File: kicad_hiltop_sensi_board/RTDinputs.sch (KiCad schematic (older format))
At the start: 0 parts

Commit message: updated sensi board for LBBC 04/09/19
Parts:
- added C1, C2, C3, C30, C31, C32, C33, C4, C5, C6, C7, C8: 100n, symbol device:C
- added J10, J11, J12, J4, J5, J7, J8, J9: Screw_Terminal_01x02, symbol Connector:Screw_Terminal_01x02
- added JP10, JP2, JP4, JP8: Jumper_NC_Dual, symbol device:Jumper_NC_Dual
- added JP11, JP12, JP13, JP3, JP5, JP6, JP7, JP9: Jumper_NC_Small, symbol device:Jumper_NC_Small
- added R1, R2, R5, R6: 470, symbol device:R
- added R12, R3, R4, R7: 10k, symbol device:R
- added U10, U11, U12, U9: MAX31865, symbol Devtank:MAX31865
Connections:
- new net: R2.1, U10.1 (BIAS), U10.2 (REFIN+)
- new net: R2.2, U10.3 (REFIN-), U10.4 (ISENSOR)
- new net: C3.1, J8.2 (Pin_2), JP7.1, U10.8 (RTDIN-)
- new net: C3.2, J5.1 (Pin_1), JP5.2, U10.7 (RTDIN+)
- new net: J5.2 (Pin_2), JP4.1, JP5.1, U10.5 (FORCE+)
- new net: JP4.2, U10.6 (FORCE2)
- new net: J8.1 (Pin_1), JP7.2, U10.9 (FORCE-)
- new net: R6.1, U12.1 (BIAS), U12.2 (REFIN+)
- new net: R6.2, U12.3 (REFIN-), U12.4 (ISENSOR)
- new net: J10.2 (Pin_2), JP10.1, JP11.1, U12.5 (FORCE+)
- new net: JP10.2, U12.6 (FORCE2)
- new net: C30.2, J10.1 (Pin_1), JP11.2, U12.7 (RTDIN+)
- new net: C30.1, J12.2 (Pin_2), JP13.1, U12.8 (RTDIN-)
- new net: J12.1 (Pin_1), JP13.2, U12.9 (FORCE-)
- new net: R1.1, U9.1 (BIAS), U9.2 (REFIN+)
- new net: R1.2, U9.3 (REFIN-), U9.4 (ISENSOR)
- new net: J4.2 (Pin_2), JP2.1, JP3.1, U9.5 (FORCE+)
- new net: JP2.2, U9.6 (FORCE2)
- new net: C1.2, J4.1 (Pin_1), JP3.2, U9.7 (RTDIN+)
- new net: C1.1, J7.2 (Pin_2), JP6.1, U9.8 (RTDIN-)
- new net: J7.1 (Pin_1), JP6.2, U9.9 (FORCE-)
- new net: R5.1, U11.1 (BIAS), U11.2 (REFIN+)
- new net: R5.2, U11.3 (REFIN-), U11.4 (ISENSOR)
- new net: J9.2 (Pin_2), JP8.1, JP9.1, U11.5 (FORCE+)
- new net: JP8.2, U11.6 (FORCE2)
- new net: C7.2, J9.1 (Pin_1), JP9.2, U11.7 (RTDIN+)
- new net: C7.1, J11.2 (Pin_2), JP12.1, U11.8 (RTDIN-)
- new net: J11.1 (Pin_1), JP12.2, U11.9 (FORCE-)
- new net +3V3: C2.1, C31.1, C32.1, C33.1, C4.1, C5.1, C6.1, C8.1, R12.1, R3.1, R4.1, R7.1, U10.19 (DVDD), U10.20 (VDD), U11.19 (DVDD), U11.20 (VDD), U12.19 (DVDD), U12.20 (VDD), U9.19 (DVDD), U9.20 (VDD)
- new net CS1: R4.2, U10.13 (~CS)
- new net CS2: R12.2, U12.13 (~CS)
- new net CS3: R3.2, U9.13 (~CS)
- new net CS4: R7.2, U11.13 (~CS)
- new net GND: C2.2, C31.2, C32.2, C33.2, C4.2, C5.2, C6.2, C8.2, JP10.3, JP2.3, JP4.3, JP8.3, U10.10 (GND2), U10.15 (DGND), U10.16 (GND1), U10.21 (EP), U11.10 (GND2), U11.15 (DGND), U11.16 (GND1), U11.21 (EP), U12.10 (GND2), U12.15 (DGND), U12.16 (GND1), U12.21 (EP), U9.10 (GND2), U9.15 (DGND), U9.16 (GND1), U9.21 (EP)
- new net INT1: U10.18 (~DRDY)
- new net INT2: U12.18 (~DRDY)
- new net INT3: U9.18 (~DRDY)
- new net INT4: U11.18 (~DRDY)
- new net MISO: U10.14 (SDO), U11.14 (SDO), U12.14 (SDO), U9.14 (SDO)
- new net MOSI: U10.11 (SDI), U11.11 (SDI), U12.11 (SDI), U9.11 (SDI)
- new net SCK: U10.12 (SCLK), U11.12 (SCLK), U12.12 (SCLK), U9.12 (SCLK)
- no-connect marks 0 -> 4

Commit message: LBBC sensi board upto date schematic and footprints
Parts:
- C1, C2, C3, C30, C31, C32, C33, C4, C5, C6, C7, C8: footprint (none) -> Capacitor_SMD:C_0603_1608Metric
- R1, R12, R2, R3, R4, R5, R6, R7: footprint (none) -> Resistor_SMD:R_0603_1608Metric
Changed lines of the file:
@@
 $Descr A3 16535 11693
 encoding utf-8
-Sheet 8 11
+Sheet 7 11
 Title ""
 Date ""
@@
 F 0 "C4" H 3765 1546 50  0000 L CNN
 F 1 "100n" H 3765 1455 50  0000 L CNN
-F 2 "" H 3688 1350 50  0001 C CNN
+F 2 "Capacitor_SMD:C_0603_1608Metric" H 3688 1350 50  0001 C CNN
 F 3 "" H 3650 1500 50  0001 C CNN
 	1    3650 1500
@@
 F 0 "C6" H 4215 1546 50  0000 L CNN
 F 1 "100n" H 4215 1455 50  0000 L CNN
-F 2 "" H 4138 1350 50  0001 C CNN
+F 2 "Capacitor_SMD:C_0603_1608Metric" H 4138 1350 50  0001 C CNN
 F 3 "" H 4100 1500 50  0001 C CNN
 	1    4100 1500
@@
 F 0 "R2" H 2320 2646 50  0000 L CNN
 F 1 "470" H 2320 2555 50  0000 L CNN
-F 2 "" V 2180 2600 50  0001 C CNN
+F 2 "Resistor_SMD:R_0603_1608Metric" V 2180 2600 50  0001 C CNN
 F 3 "" H 2250 2600 50  0001 C CNN
 	1    2250 2600
@@
 F 0 "R4" H 4670 1546 50  0000 L CNN
 F 1 "10k" H 4670 1455 50  0000 L CNN
-F 2 "" V 4530 1500 50  0001 C CNN
+F 2 "Resistor_SMD:R_0603_1608Metric" V 4530 1500 50  0001 C CNN
 F 3 "" H 4600 1500 50  0001 C CNN
 	1    4600 1500
@@
 F 0 "C3" V 3150 4100 50  0000 C CNN
 F 1 "100n" V 3239 4050 50  0000 C CNN
-F 2 "" H 3438 3900 50  0001 C CNN
+F 2 "Capacitor_SMD:C_0603_1608Metric" H 3438 3900 50  0001 C CNN
 F 3 "" H 3400 4050 50  0001 C CNN
 	1    3400 4050
@@
 F 0 "C31" H 7015 1596 50  0000 L CNN
 F 1 "100n" H 7015 1505 50  0000 L CNN
-F 2 "" H 6938 1400 50  0001 C CNN
+F 2 "Capacitor_SMD:C_0603_1608Metric" H 6938 1400 50  0001 C CNN
 F 3 "" H 6900 1550 50  0001 C CNN
 	1    6900 1550
@@
 F 0 "C33" H 7465 1596 50  0000 L CNN
 F 1 "100n" H 7465 1505 50  0000 L CNN
-F 2 "" H 7388 1400 50  0001 C CNN
+F 2 "Capacitor_SMD:C_0603_1608Metric" H 7388 1400 50  0001 C CNN
 F 3 "" H 7350 1550 50  0001 C CNN
 	1    7350 1550
@@
 F 0 "R6" H 5570 2696 50  0000 L CNN
 F 1 "470" H 5570 2605 50  0000 L CNN
-F 2 "" V 5430 2650 50  0001 C CNN
+F 2 "Resistor_SMD:R_0603_1608Metric" V 5430 2650 50  0001 C CNN
 F 3 "" H 5500 2650 50  0001 C CNN
 	1    5500 2650
@@
 F 0 "R12" H 7920 1596 50  0000 L CNN
 F 1 "10k" H 7920 1505 50  0000 L CNN
-F 2 "" V 7780 1550 50  0001 C CNN
+F 2 "Resistor_SMD:R_0603_1608Metric" V 7780 1550 50  0001 C CNN
 F 3 "" H 7850 1550 50  0001 C CNN
 	1    7850 1550
@@
 F 0 "C30" V 6400 4150 50  0000 C CNN
 F 1 "100n" V 6489 4100 50  0000 C CNN
-F 2 "" H 6688 3950 50  0001 C CNN
+F 2 "Capacitor_SMD:C_0603_1608Metric" H 6688 3950 50  0001 C CNN
 F 3 "" H 6650 4100 50  0001 C CNN
 	1    6650 4100
@@
 F 0 "C2" H 3365 6196 50  0000 L CNN
 F 1 "100n" H 3365 6105 50  0000 L CNN
-F 2 "" H 3288 6000 50  0001 C CNN
+F 2 "Capacitor_SMD:C_0603_1608Metric" H 3288 6000 50  0001 C CNN
 F 3 "" H 3250 6150 50  0001 C CNN
 	1    3250 6150
@@
 F 0 "C5" H 3815 6196 50  0000 L CNN
 F 1 "100n" H 3815 6105 50  0000 L CNN
-F 2 "" H 3738 6000 50  0001 C CNN
+F 2 "Capacitor_SMD:C_0603_1608Metric" H 3738 6000 50  0001 C CNN
 F 3 "" H 3700 6150 50  0001 C CNN
 	1    3700 6150
@@
 F 0 "R1" H 1920 7296 50  0000 L CNN
 F 1 "470" H 1920 7205 50  0000 L CNN
-F 2 "" V 1780 7250 50  0001 C CNN
+F 2 "Resistor_SMD:R_0603_1608Metric" V 1780 7250 50  0001 C CNN
 F 3 "" H 1850 7250 50  0001 C CNN
 	1    1850 7250
@@
 F 0 "R3" H 4270 6196 50  0000 L CNN
 F 1 "10k" H 4270 6105 50  0000 L CNN
-F 2 "" V 4130 6150 50  0001 C CNN
+F 2 "Resistor_SMD:R_0603_1608Metric" V 4130 6150 50  0001 C CNN
 F 3 "" H 4200 6150 50  0001 C CNN
 	1    4200 6150
@@
 F 0 "C1" V 2750 8750 50  0000 C CNN
 F 1 "100n" V 2839 8700 50  0000 C CNN
-F 2 "" H 3038 8550 50  0001 C CNN
+F 2 "Capacitor_SMD:C_0603_1608Metric" H 3038 8550 50  0001 C CNN
 F 3 "" H 3000 8700 50  0001 C CNN
 	1    3000 8700
@@
 F 0 "C8" H 6615 6246 50  0000 L CNN
 F 1 "100n" H 6615 6155 50  0000 L CNN
-F 2 "" H 6538 6050 50  0001 C CNN
+F 2 "Capacitor_SMD:C_0603_1608Metric" H 6538 6050 50  0001 C CNN
 F 3 "" H 6500 6200 50  0001 C CNN
 	1    6500 6200
@@
 F 0 "C32" H 7065 6246 50  0000 L CNN
 F 1 "100n" H 7065 6155 50  0000 L CNN
-F 2 "" H 6988 6050 50  0001 C CNN
+F 2 "Capacitor_SMD:C_0603_1608Metric" H 6988 6050 50  0001 C CNN
 F 3 "" H 6950 6200 50  0001 C CNN
 	1    6950 6200
@@
 F 0 "R5" H 5170 7346 50  0000 L CNN
 F 1 "470" H 5170 7255 50  0000 L CNN
-F 2 "" V 5030 7300 50  0001 C CNN
+F 2 "Resistor_SMD:R_0603_1608Metric" V 5030 7300 50  0001 C CNN
 F 3 "" H 5100 7300 50  0001 C CNN
 	1    5100 7300
@@
 F 0 "R7" H 7520 6246 50  0000 L CNN
 F 1 "10k" H 7520 6155 50  0000 L CNN
-F 2 "" V 7380 6200 50  0001 C CNN
+F 2 "Resistor_SMD:R_0603_1608Metric" V 7380 6200 50  0001 C CNN
 F 3 "" H 7450 6200 50  0001 C CNN
 	1    7450 6200
@@
 F 0 "C7" V 6000 8800 50  0000 C CNN
 F 1 "100n" V 6089 8750 50  0000 C CNN
-F 2 "" H 6288 8600 50  0001 C CNN
+F 2 "Capacitor_SMD:C_0603_1608Metric" H 6288 8600 50  0001 C CNN
 F 3 "" H 6250 8750 50  0001 C CNN
 	1    6250 8750

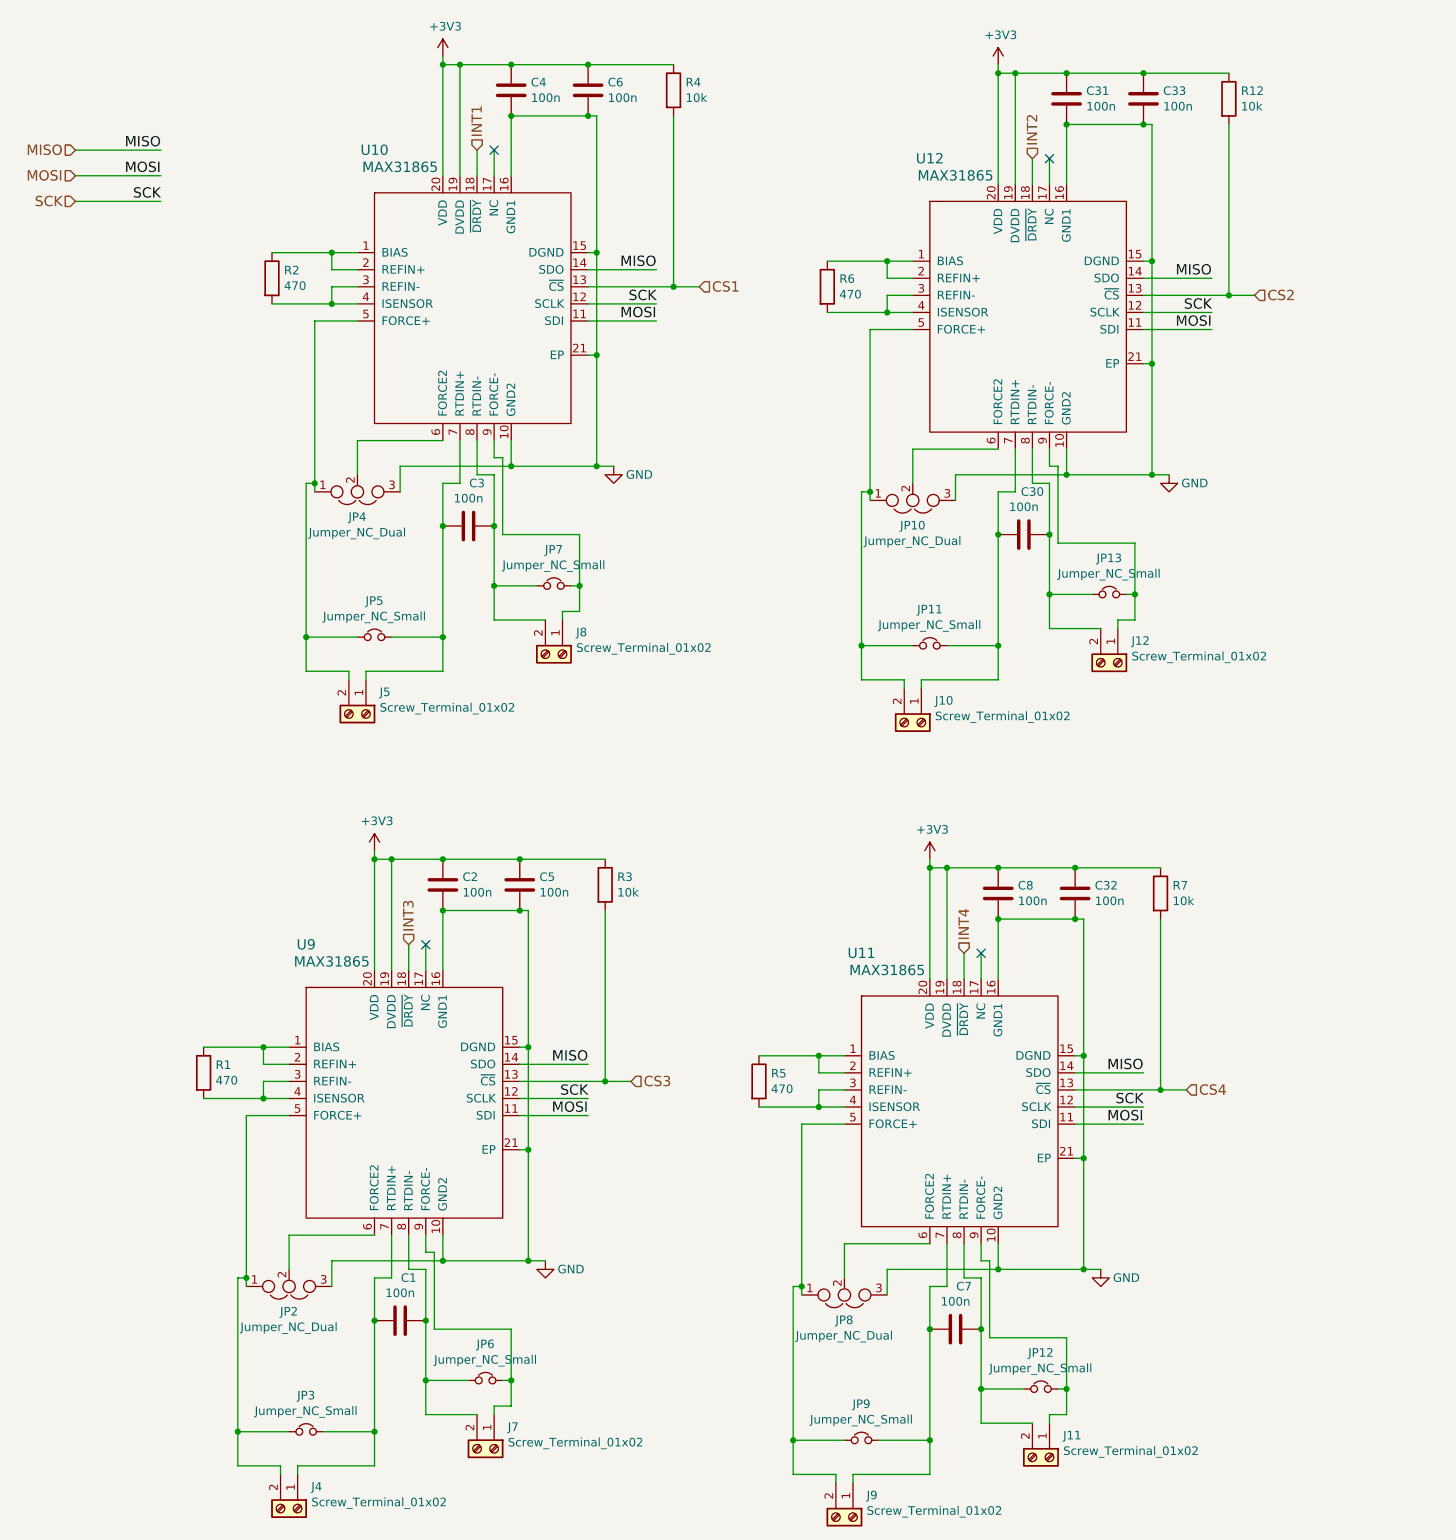
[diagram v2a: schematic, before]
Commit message: All sensors connected to STM Microcontroller
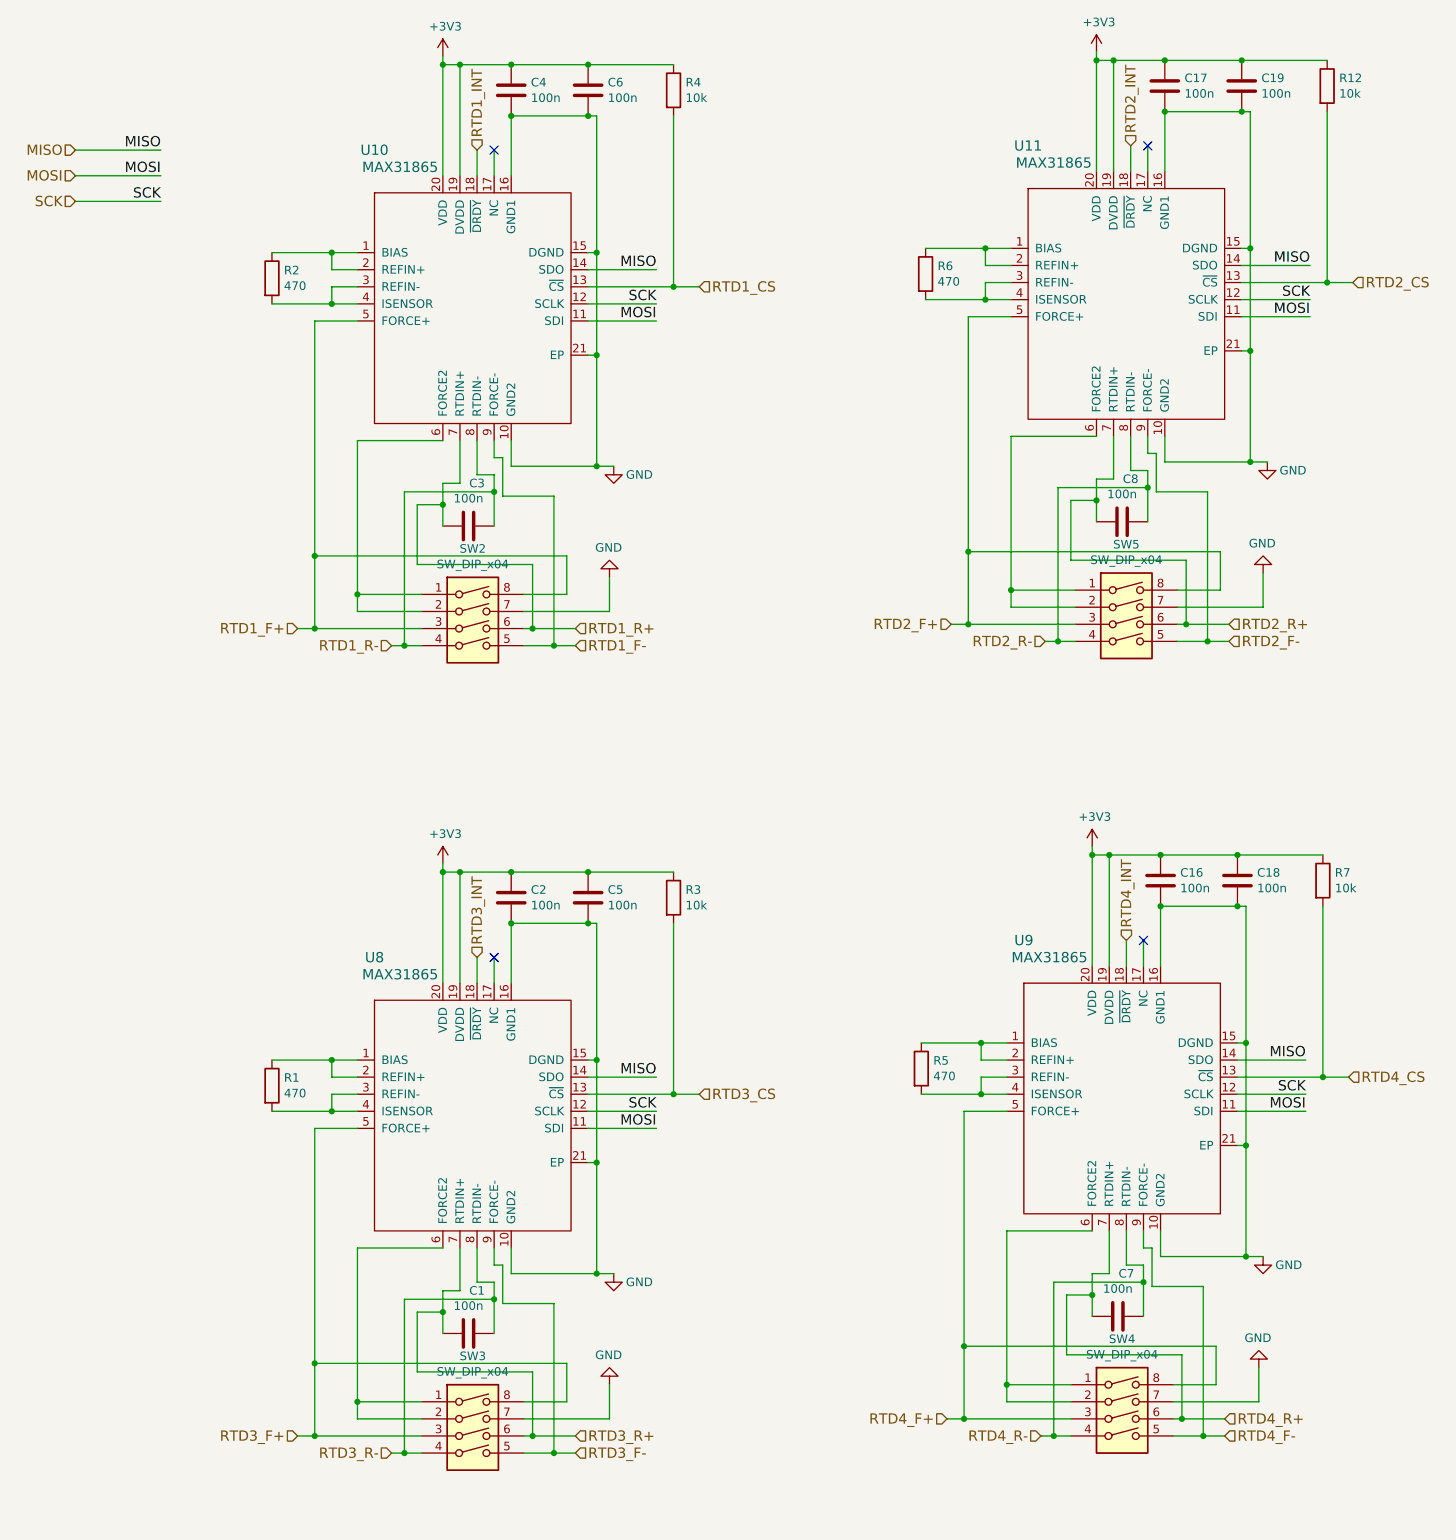
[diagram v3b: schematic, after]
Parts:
- removed C30, C31, C32, C33: 100n, Capacitor_SMD:C_0603_1608Metric, symbol device:C
- removed J10, J11, J12, J4, J5, J7, J8, J9: Screw_Terminal_01x02, symbol Connector:Screw_Terminal_01x02
- removed JP10, JP2, JP4, JP8: Jumper_NC_Dual, symbol device:Jumper_NC_Dual
- removed JP11, JP12, JP13, JP3, JP5, JP6, JP7, JP9: Jumper_NC_Small, symbol device:Jumper_NC_Small
- removed U12: MAX31865, symbol Devtank:MAX31865
- added C16, C17, C18, C19: 100n, Capacitor_SMD:C_0603_1608Metric, symbol device:C
- added SW2, SW3, SW4, SW5: SW_DIP_x04, symbol Switch:SW_DIP_x04
- added U8: MAX31865, symbol Devtank:MAX31865
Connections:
- net +3V3: now also C16.1, C17.1, C18.1, C19.1, U8.19 (DVDD), U8.20 (VDD); no longer C8.1
- net GND: now also C16.2, C17.2, C18.2, C19.2, SW2.7, SW3.7, SW4.7, SW5.7, U8.10 (GND2), U8.15 (DGND), U8.16 (GND1), U8.21 (EP); no longer C8.2
- net MISO: now also U8.14 (SDO)
- net MOSI: now also U8.11 (SDI)
- net SCK: now also U8.12 (SCLK)
- net RTD1_R-: now reaches C3.1, U10.8 (RTDIN-)
- net RTD1_R-: now also SW2.4
- net RTD1_R+: now reaches C3.2, U10.7 (RTDIN+)
- net RTD1_R+: now also SW2.6
- net RTD1_F+: now reaches U10.5 (FORCE+)
- net RTD1_F+: now also SW2.3, SW2.8
- net at U10.6 (FORCE2): now also SW2.1, SW2.2
- net RTD1_F-: now reaches U10.9 (FORCE-)
- net RTD1_F-: now also SW2.5
- net at R6.1: now also U11.1 (BIAS), U11.2 (REFIN+)
- net at R6.2: now also U11.3 (REFIN-), U11.4 (ISENSOR)
- net at U9.1 (BIAS), U9.2 (REFIN+): now also R5.1; no longer R1.1
- net at U9.3 (REFIN-), U9.4 (ISENSOR): now also R5.2; no longer R1.2
- net RTD4_F+: now reaches U9.5 (FORCE+)
- net RTD4_F+: now also SW4.3, SW4.8
- net at U9.6 (FORCE2): now also SW4.1, SW4.2
- net RTD3_R+: now reaches C1.2
- net RTD3_R+: now also SW3.6, U8.7 (RTDIN+); no longer U9.7 (RTDIN+)
- net RTD3_R-: now reaches C1.1
- net RTD3_R-: now also SW3.4, U8.8 (RTDIN-); no longer U9.8 (RTDIN-)
- net RTD4_F-: now reaches U9.9 (FORCE-)
- net RTD4_F-: now also SW4.5
- net RTD2_F+: now reaches U11.5 (FORCE+)
- net RTD2_F+: now also SW5.3, SW5.8
- net at U11.6 (FORCE2): now also SW5.1, SW5.2
- net RTD2_R+: now reaches U11.7 (RTDIN+)
- net RTD2_R+: now also C8.2, SW5.6; no longer C7.2
- net RTD2_R-: now reaches U11.8 (RTDIN-)
- net RTD2_R-: now also C8.1, SW5.4; no longer C7.1
- net RTD2_F-: now reaches U11.9 (FORCE-)
- net RTD2_F-: now also SW5.5
- net CS1 renamed RTD1_CS
- net CS2 renamed RTD2_CS
- net RTD2_CS: now also U11.13 (~CS)
- net CS3 renamed RTD3_CS
- net RTD3_CS: now also U8.13 (~CS); no longer U9.13 (~CS)
- net CS4 renamed RTD4_CS
- net RTD4_CS: now also U9.13 (~CS); no longer U11.13 (~CS)
- net INT1 renamed RTD1_INT
- net INT3 renamed RTD4_INT
- net INT4 renamed RTD2_INT
- new net: R1.1, U8.1 (BIAS), U8.2 (REFIN+)
- new net: R1.2, U8.3 (REFIN-), U8.4 (ISENSOR)
- new net: SW3.1, SW3.2, U8.6 (FORCE2)
- new net RTD3_F+: SW3.3, SW3.8, U8.5 (FORCE+)
- new net RTD3_F-: SW3.5, U8.9 (FORCE-)
- new net RTD3_INT: U8.18 (~DRDY)
- new net RTD4_R+: C7.2, SW4.6, U9.7 (RTDIN+)
- new net RTD4_R-: C7.1, SW4.4, U9.8 (RTDIN-)
